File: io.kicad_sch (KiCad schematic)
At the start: 21 parts, among them J30 FTDI-MCU, J31 UART-DALI, J40 A10, J41 A5-1, J42 A5-2, J43 A2-1, J44 A2-2, J45 A2-3, J46 A2-4, J47 A2-5, J50 D8, J51 D4-1, J52 D4-2, J53 D2-1, J54 D2-2, J55 D2-3, J56 D2-4, J60 D1-11, J61 D1-12, J62 D1-13, J63 D1-14

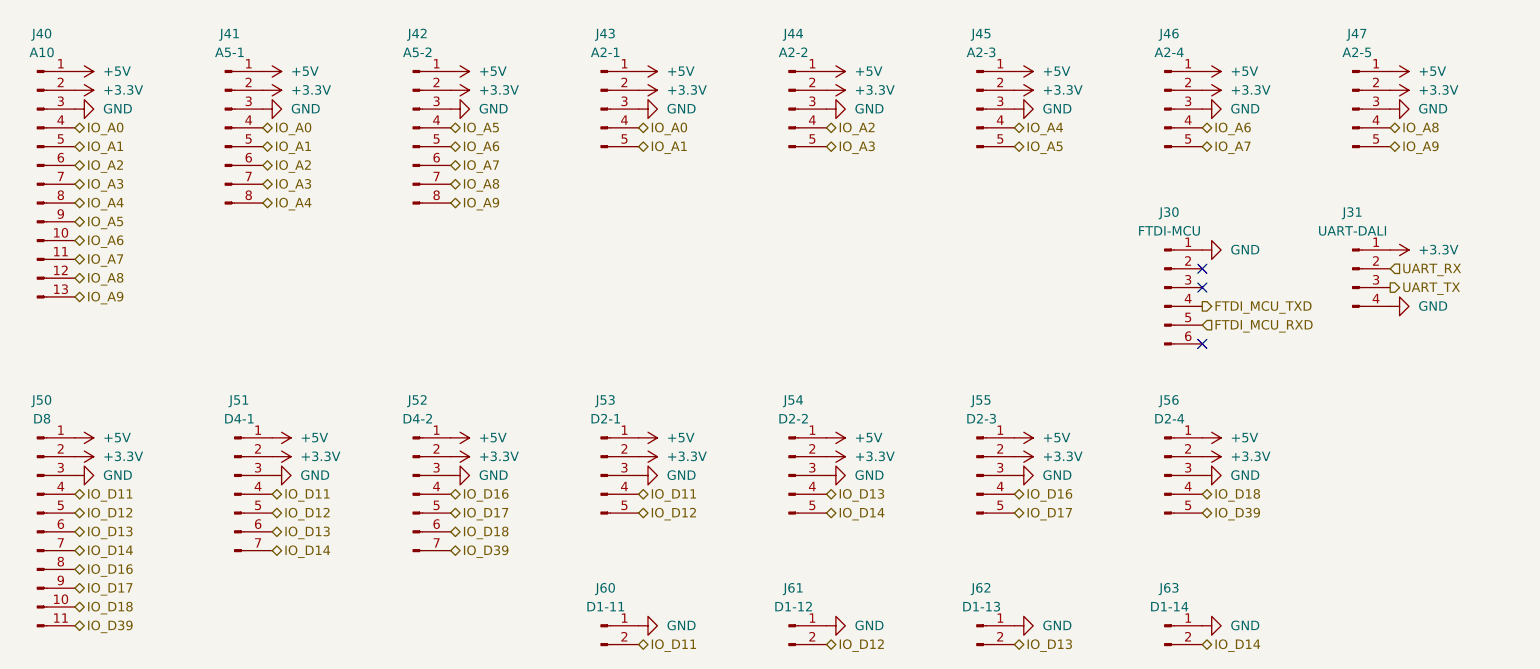
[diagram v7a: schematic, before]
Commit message: Label all the I/O pins
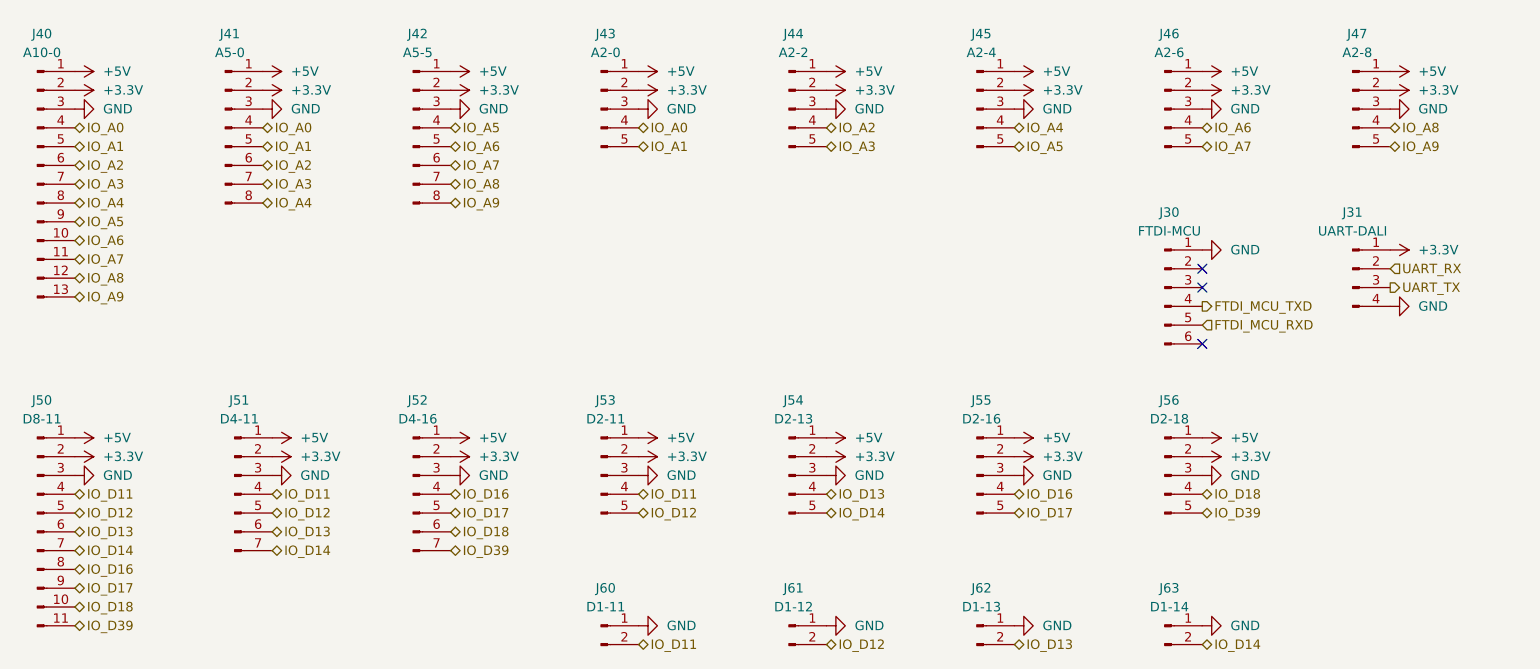
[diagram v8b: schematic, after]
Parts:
- J40: value A10 -> A10-0
- J41: value A5-1 -> A5-0
- J42: value A5-2 -> A5-5
- J43: value A2-1 -> A2-0
- J45: value A2-3 -> A2-4
- J46: value A2-4 -> A2-6
- J47: value A2-5 -> A2-8
- J50: value D8 -> D8-11
- J51: value D4-1 -> D4-11
- J52: value D4-2 -> D4-16
- J53: value D2-1 -> D2-11
- J54: value D2-2 -> D2-13
- J55: value D2-3 -> D2-16
- J56: value D2-4 -> D2-18
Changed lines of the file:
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@@
 			)
 		)
-		(property "Value" "A2-4"
+		(property "Value" "A2-6"
 			(at 158.115 8.89 0)
 			(effects
@@
 			)
 		)
-		(property "Value" "D2-1"
+		(property "Value" "D2-11"
 			(at 81.915 58.42 0)
 			(effects
@@
 			)
 		)
-		(property "Value" "D2-2"
+		(property "Value" "D2-13"
 			(at 107.315 58.42 0)
 			(effects
@@
 			)
 		)
-		(property "Value" "A2-1"
+		(property "Value" "A2-0"
 			(at 81.915 8.89 0)
 			(effects
@@
 			)
 		)
-		(property "Value" "A10"
+		(property "Value" "A10-0"
 			(at 5.715 8.89 0)
 			(effects
@@
 			)
 		)
-		(property "Value" "A2-5"
+		(property "Value" "A2-8"
 			(at 183.515 8.89 0)
 			(effects
@@
 			)
 		)
-		(property "Value" "D4-2"
+		(property "Value" "D4-16"
 			(at 56.515 58.42 0)
 			(effects
@@
 			)
 		)
-		(property "Value" "A5-2"
+		(property "Value" "A5-5"
 			(at 56.515 8.89 0)
 			(effects
@@
 			)
 		)
-		(property "Value" "D2-3"
+		(property "Value" "D2-16"
 			(at 132.715 58.42 0)
 			(effects
@@
 			)
 		)
-		(property "Value" "D8"
+		(property "Value" "D8-11"
 			(at 5.715 58.42 0)
 			(effects
@@
 			)
 		)
-		(property "Value" "A5-1"
+		(property "Value" "A5-0"
 			(at 31.115 8.89 0)
 			(effects
@@
 			)
 		)
-		(property "Value" "D4-1"
+		(property "Value" "D4-11"
 			(at 32.385 58.42 0)
 			(effects
@@
 			)
 		)
-		(property "Value" "D2-4"
+		(property "Value" "D2-18"
 			(at 158.115 58.42 0)
 			(effects
@@
 			)
 		)
-		(property "Value" "A2-3"
+		(property "Value" "A2-4"
 			(at 132.715 8.89 0)
 			(effects
